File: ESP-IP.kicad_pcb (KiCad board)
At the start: 4 copper layers, 50 x 25 mm, 41 parts, among them J1 Serial and power, J2 Programming Pads, J3 Comms and power, Q1 L78M05ABDT-TR, Q2 MMBT5551L, SW1 SW_Push, SW2 SW_Push, U1 ESP32-WROOM-32U, U3 TXS0102DCU, U4 AMS1117-3.3

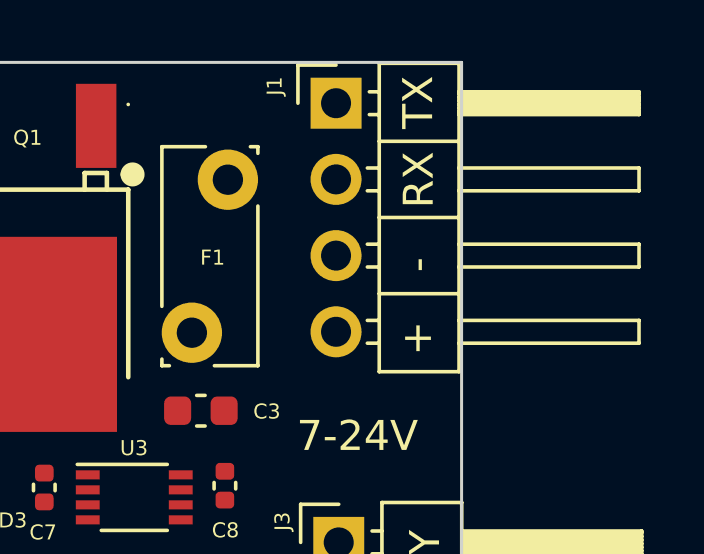
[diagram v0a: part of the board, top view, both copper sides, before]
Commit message: chore: switch header back for serial and standardise labels
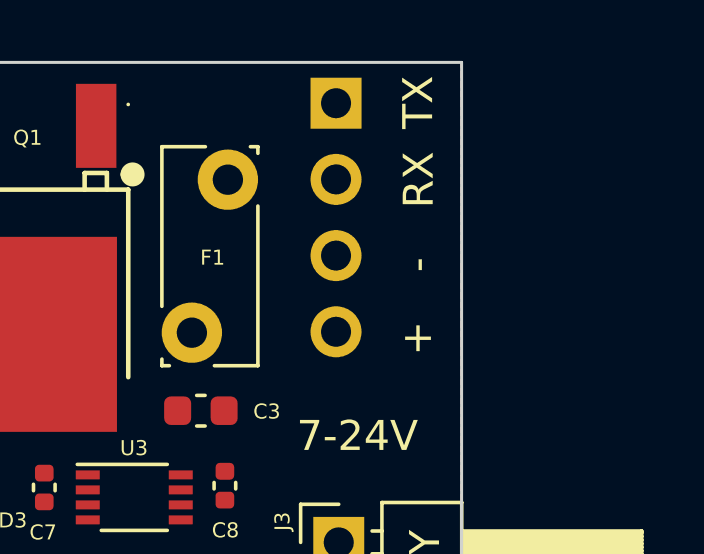
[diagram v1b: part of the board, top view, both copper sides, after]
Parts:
- J1: footprint Connector_PinHeader_2.54mm:PinHeader_1x04_P2.54mm_Horizontal -> Connector_PinHeader_2.54mm:PinHeader_1x04_P2.54mm_Vertical; moved to B.Cu
- turned J1 to 180 degrees
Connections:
- net DSC Green renamed DSC_GREEN
- net DSC Yellow renamed DSC_YELLOW
- net dscClock renamed DSC_CLOCK
- net dscRead renamed DSC_READ
- net dscWrite renamed DSC_WRITE

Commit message: chore: initial routing
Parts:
- J1: footprint Connector_PinHeader_2.54mm:PinHeader_1x04_P2.54mm_Vertical -> Connector_PinSocket_2.54mm:PinSocket_1x04_P2.54mm_Vertical
- moved D2 0.63 mm to (85.0, 100.4)
- moved D1 0.61 mm to (80.6, 100.4)
- moved R2 0.57 mm to (88.7, 100.4)
- moved R1 0.50 mm to (77.7, 100.4)
- moved R12 0.41 mm to (113.9, 115.8)
- moved C10 0.27 mm to (104.2, 114.4)
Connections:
- U1 pad 11: unconnected-(U1-IO26-Pad11) -> WIFI_STATUS
- U1 pad 16: WIFI_STATUS -> unconnected-(U1-IO13-Pad16)
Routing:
- net TX_ESP: track 0.00 -> 50.7 mm, vias 0 -> 2
- net RX_ESP: track 0.00 -> 40.8 mm, vias 0 -> 2
- net EN: track 0.00 -> 38.8 mm, vias 0 -> 2
- net DSC_CLOCK: track 0.00 -> 37.9 mm, vias 0 -> 2
- net DSC_WRITE: track 0.00 -> 37.6 mm, vias 0 -> 2
- net DSC_READ: track 0.00 -> 33.9 mm, vias 0 -> 2
- net +3V3: track 0.00 -> 33.7 mm, vias 0 -> 8
- net +5V: track 0.00 -> 28.3 mm, vias 0 -> 2
- net IO0: track 0.00 -> 26.4 mm, vias 0 -> 2
- net +BATT: track 0.00 -> 24.8 mm
- net DSC_GREEN: track 0.00 -> 15.2 mm, vias 0 -> 1
- net DSC_YELLOW: track 0.00 -> 11.5 mm
- net Net-(Q1-IN): track 0.00 -> 5.13 mm
- net Net-(Q2-B): track 0.00 -> 3.81 mm
- net AP_STATUS: track 0.00 -> 2.80 mm
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
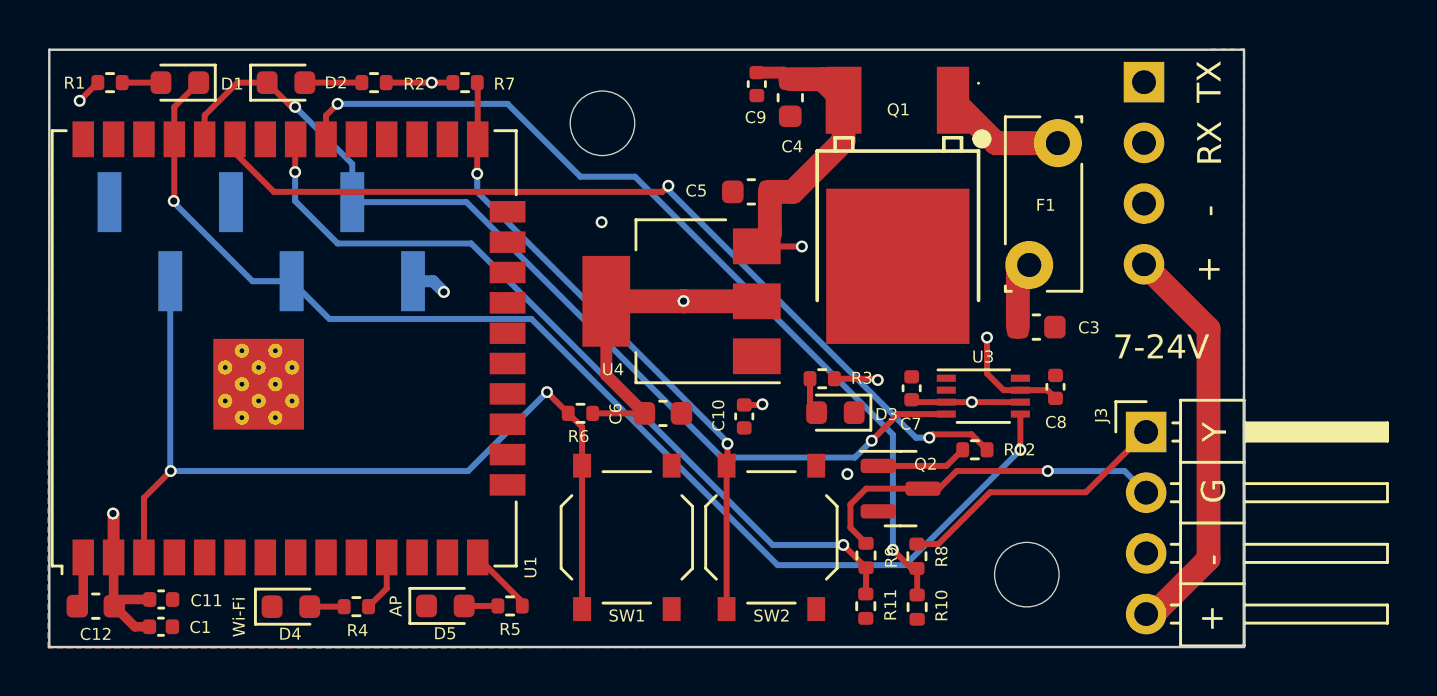
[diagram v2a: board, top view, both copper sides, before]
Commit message: chore: swap labels of rx and tx on pin socket
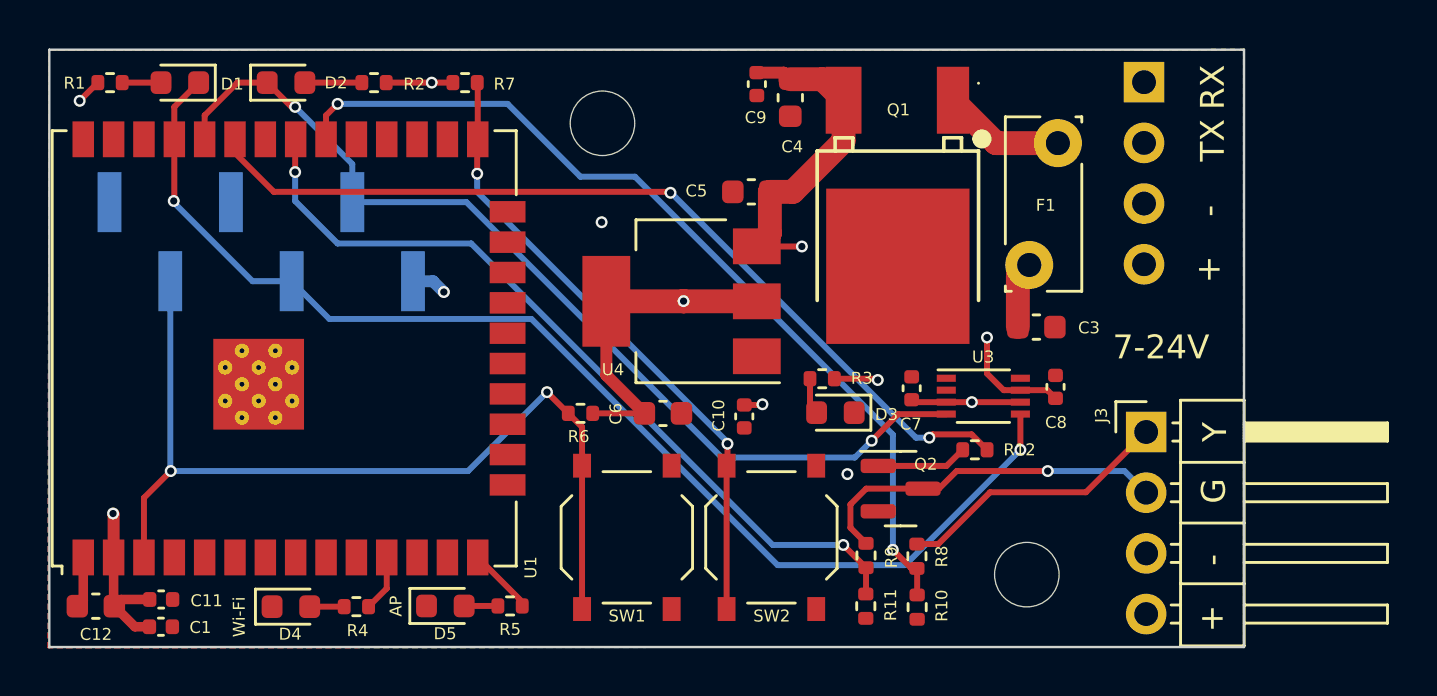
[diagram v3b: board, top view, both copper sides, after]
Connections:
- J1 pad 1: TX_OUT -> RX_OUT
- J1 pad 2: RX_OUT -> TX_OUT
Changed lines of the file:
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@@
       (stroke (width 0.1) (type solid)) (layer "B.Fab"))
     (pad "1" thru_hole rect (at 0 0 180) (size 1.7 1.7) (drill 1) (layers "*.Cu" "*.Mask")
-      (net 36 "TX_OUT") (pinfunction "Pin_1") (pintype "passive"))
+      (net 32 "RX_OUT") (pinfunction "Pin_1") (pintype "passive"))
     (pad "2" thru_hole oval (at 0 -2.54 180) (size 1.7 1.7) (drill 1) (layers "*.Cu" "*.Mask")
-      (net 32 "RX_OUT") (pinfunction "Pin_2") (pintype "passive"))
+      (net 36 "TX_OUT") (pinfunction "Pin_2") (pintype "passive"))
     (pad "3" thru_hole oval (at 0 -5.08 180) (size 1.7 1.7) (drill 1) (layers "*.Cu" "*.Mask")
       (net 1 "GND") (pinfunction "Pin_3") (pintype "passive"))
@@
     (effects (font (size 1 1) (thickness 0.15)) (justify left bottom mirror))
   )
-  (gr_text "TX" (at 123.05 101.3 -90) (layer "B.SilkS")
+  (gr_text "TX" (at 123.126 103.73 -90) (layer "B.SilkS")
     (effects (font (size 1 1) (thickness 0.15)) (justify left bottom mirror))
   )
-  (gr_text "RX\n" (at 123.03 103.94 -90) (layer "B.SilkS")
+  (gr_text "RX\n" (at 123.126 101.571 -90) (layer "B.SilkS")
     (effects (font (size 1 1) (thickness 0.15)) (justify left bottom mirror))
   )
@@
     (effects (font (size 1 1) (thickness 0.15)) (justify left bottom))
   )
-  (gr_text "TX" (at 124.26 101.27 90) (layer "F.SilkS")
+  (gr_text "TX" (at 124.396 103.73 90) (layer "F.SilkS")
     (effects (font (size 1 1) (thickness 0.15)) (justify left bottom))
   )
@@
     (effects (font (size 1 1) (thickness 0.15)) (justify left bottom))
   )
-  (gr_text "RX\n" (at 124.28 103.91 90) (layer "F.SilkS")
+  (gr_text "RX\n" (at 124.396 101.571 90) (layer "F.SilkS")
     (effects (font (size 1 1) (thickness 0.15)) (justify left bottom))
   )
@@
   (segment (start 85.407 105.381) (end 85.407 104.1715) (width 0.25) (layer "B.Cu") (net 34))
   (segment (start 92.774 107.16) (end 87.186 107.16) (width 0.25) (layer "B.Cu") (net 34))
-  (segment (start 84.518 105) (end 100.774 105) (width 0.25) (layer "F.Cu") (net 35))
-  (segment (start 82.89 103.372) (end 84.518 105) (width 0.25) (layer "F.Cu") (net 35))
+  (segment (start 101.078466 105) (end 84.518 105) (width 0.25) (layer "F.Cu") (net 35))
+  (segment (start 84.518 105) (end 82.89 103.372) (width 0.25) (layer "F.Cu") (net 35))
   (segment (start 112.087 115.15) (end 113.72 115.15) (width 0.25) (layer "F.Cu") (net 35))
-  (segment (start 100.774 105) (end 101.028 104.746) (width 0.25) (layer "F.Cu") (net 35))
-  (segment (start 82.89 102.8) (end 82.89 103.372) (width 0.25) (layer "F.Cu") (net 35))
+  (segment (start 101.116733 105.038267) (end 101.078466 105) (width 0.25) (layer "F.Cu") (net 35))
+  (segment (start 82.89 103.372) (end 82.89 102.8) (width 0.25) (layer "F.Cu") (net 35))
   (segment (start 111.95 115.287) (end 112.087 115.15) (width 0.25) (layer "F.Cu") (net 35))
   (segment (start 113.72 115.15) (end 114.365 115.795) (width 0.25) (layer "F.Cu") (net 35))
-  (via (at 101.028 104.746) (size 0.5) (drill 0.3) (layers "F.Cu" "B.Cu") (net 35))
+  (via (at 101.116733 105.038267) (size 0.5) (drill 0.3) (layers "F.Cu" "B.Cu") (net 35))
   (via (at 111.95 115.287) (size 0.5) (drill 0.3) (layers "F.Cu" "B.Cu") (net 35))
+  (segment (start 101.142094 105.038267) (end 111.390827 115.287) (width 0.25) (layer "B.Cu") (net 35))
   (segment (start 111.390827 115.287) (end 111.95 115.287) (width 0.25) (layer "B.Cu") (net 35))
-  (segment (start 101.028 104.746) (end 101.028 104.924173) (width 0.25) (layer "B.Cu") (net 35))
-  (segment (start 101.028 104.924173) (end 111.390827 115.287) (width 0.25) (layer "B.Cu") (net 35))
-  (segment (start 123.634 120.367) (end 123.634 110.729) (width 1) (layer "F.Cu") (net 37))
+  (segment (start 101.116733 105.038267) (end 101.142094 105.038267) (width 0.25) (layer "B.Cu") (net 35))
   (segment (start 121.025 122.67) (end 121.331 122.67) (width 1) (layer "F.Cu") (net 37))
-  (segment (start 121.331 122.67) (end 123.634 120.367) (width 1) (layer "F.Cu") (net 37))
   (segment (start 115.655 108.535) (end 116.13 108.06) (width 1) (layer "F.Cu") (net 37))
   (segment (start 120.905 108.06) (end 120.935 108.03) (width 1) (layer "F.Cu") (net 37))
-  (segment (start 123.634 110.729) (end 120.935 108.03) (width 1) (layer "F.Cu") (net 37))
   (segment (start 115.655 110.66) (end 115.655 108.535) (width 1) (layer "F.Cu") (net 37))
+  (segment (start 121.025 122.67) (end 118.3 119.945) (width 1) (layer "In2.Cu") (net 37))
+  (segment (start 118.3 119.945) (end 118.3 110.23) (width 1) (layer "In2.Cu") (net 37))
   (segment (start 116.13 108.06) (end 120.905 108.06) (width 1) (layer "In2.Cu") (net 37))
+  (segment (start 118.3 110.23) (end 116.13 108.06) (width 1) (layer "In2.Cu") (net 37))
   (segment (start 120.905 108.06) (end 120.935 108.03) (width 1) (layer "In2.Cu") (net 37))
   (segment (start 111.385 108.03) (end 111.355 108.06) (width 1) (layer "B.Cu") (net 37))

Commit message: FEAT: ADD FROG
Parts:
- added G***: LOGO, Images:frog, F.Cu at (84.0, 108.3)
- added G***: LOGO, Images:frog, B.Cu at (84.0, 117.7)
- moved C8 0.52 mm to (117.7, 112.9)
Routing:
- net RX_OUT: track 0.00 -> 15.9 mm
- net TX_OUT: track 0.00 -> 13.0 mm
- net IO0: track 26.4 -> 37.2 mm, vias 2 -> 3
- net +5V: track 28.3 -> 30.4 mm
- net +3V3: track 33.7 -> 35.5 mm, vias 8 -> 7
- net GND: track 2.14 -> 3.52 mm, vias 2 -> 11

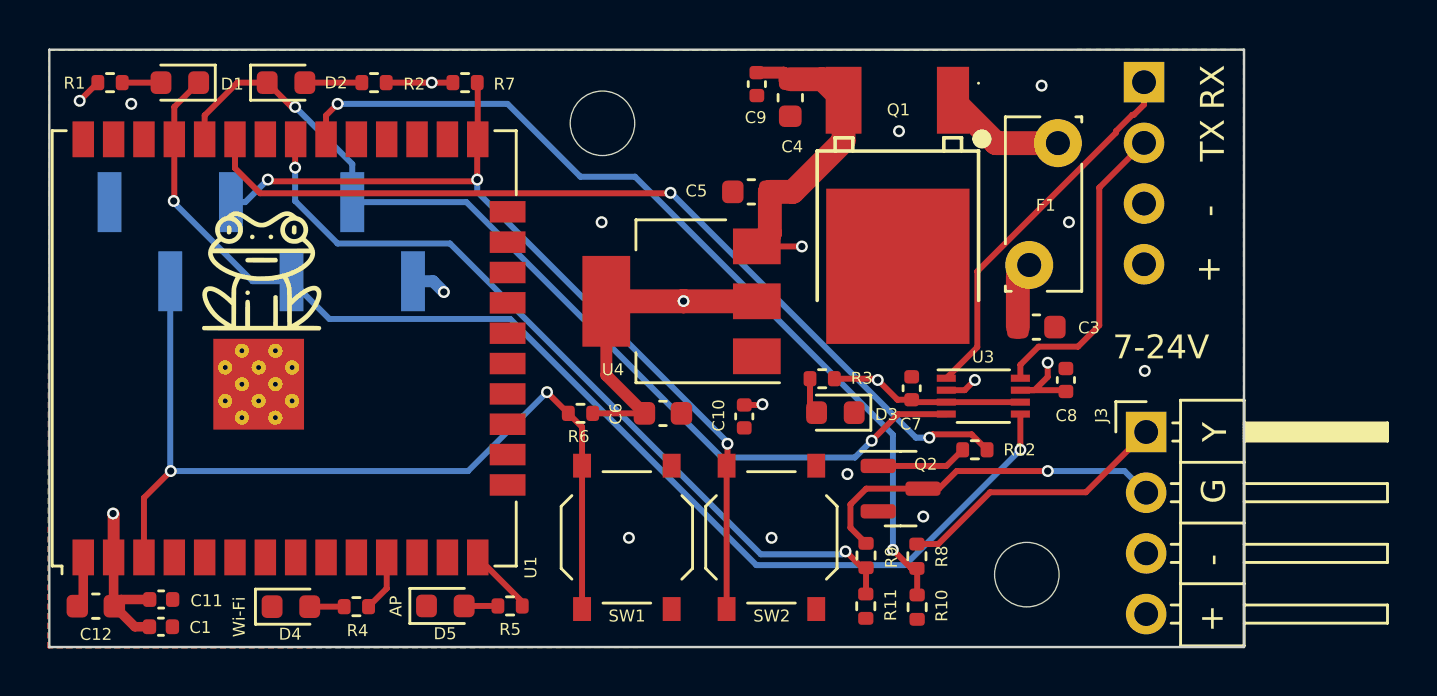
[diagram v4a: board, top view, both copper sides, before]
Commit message: cleaned up routing and minor PCB changes
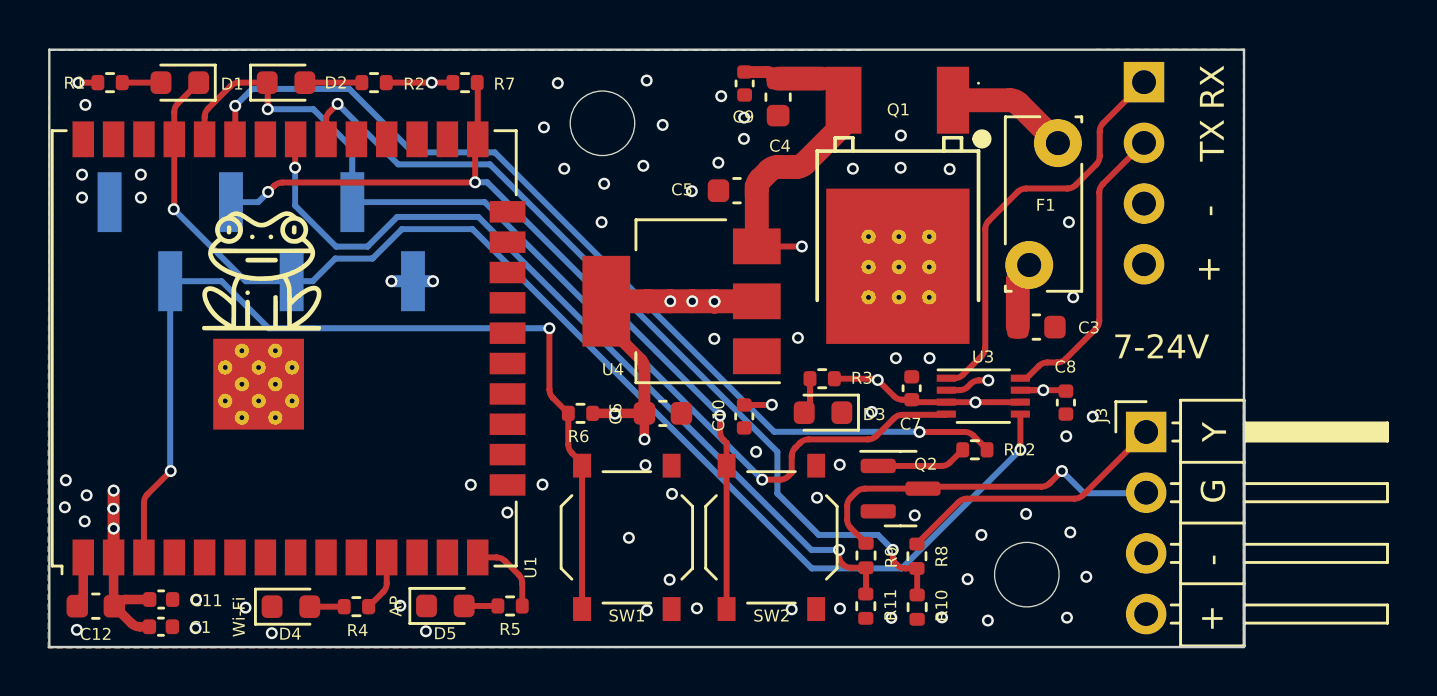
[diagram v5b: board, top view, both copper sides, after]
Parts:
- moved C8 0.95 mm to (117.7, 113.8), turned to -90 degrees
- moved C5 0.60 mm to (103.9, 105.0)
- moved D3 0.52 mm to (107.5, 114.2)
- moved C9 0.51 mm to (104.2, 100.5)
- moved C4 0.51 mm to (105.6, 101.0)
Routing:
- net +BATT: track 24.6 -> 30.9 mm
- net RX_ESP: track 40.8 -> 43.0 mm
- net TX_ESP: track 50.7 -> 52.7 mm
- net EN: track 38.8 -> 40.9 mm
- net DSC_WRITE: track 37.7 -> 39.4 mm
- net DSC_CLOCK: track 37.9 -> 36.3 mm
- net RX_OUT: track 15.9 -> 17.2 mm
- net DSC_READ: track 34.0 -> 35.3 mm
- net +3V3: track 35.5 -> 36.5 mm, vias 7 -> 15
- net +5V: track 30.4 -> 29.7 mm
- net TX_OUT: track 13.0 -> 12.3 mm
- net AP_STATUS: track 2.80 -> 3.33 mm
- net GND: track 3.52 -> 4.00 mm, vias 11 -> 67

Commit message: chore: switch rx and tx out
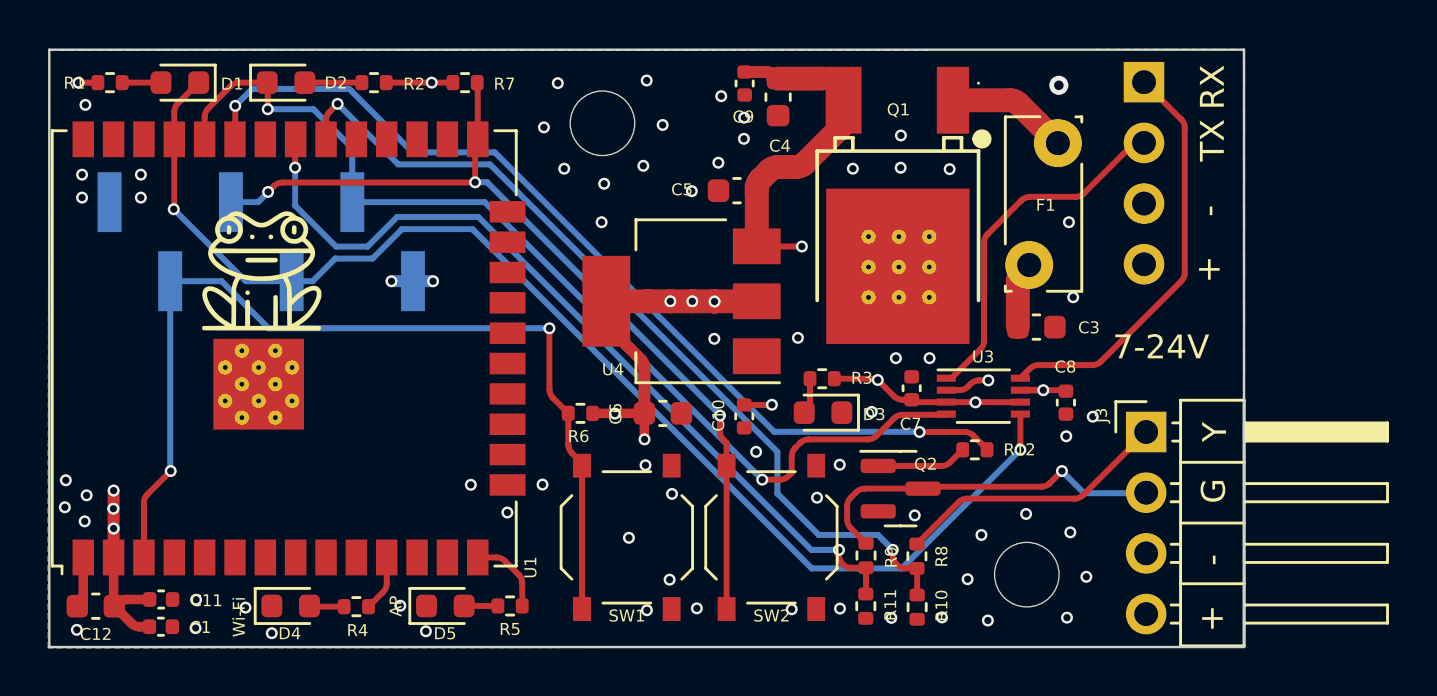
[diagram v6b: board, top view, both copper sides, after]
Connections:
- U3 pad 1: RX_OUT -> TX_OUT
- U3 pad 8: TX_OUT -> RX_OUT
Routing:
- net TX_OUT: track 12.3 -> 14.9 mm
- net GND: vias 67 -> 68
